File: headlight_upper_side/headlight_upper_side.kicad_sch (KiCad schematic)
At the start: 22 parts

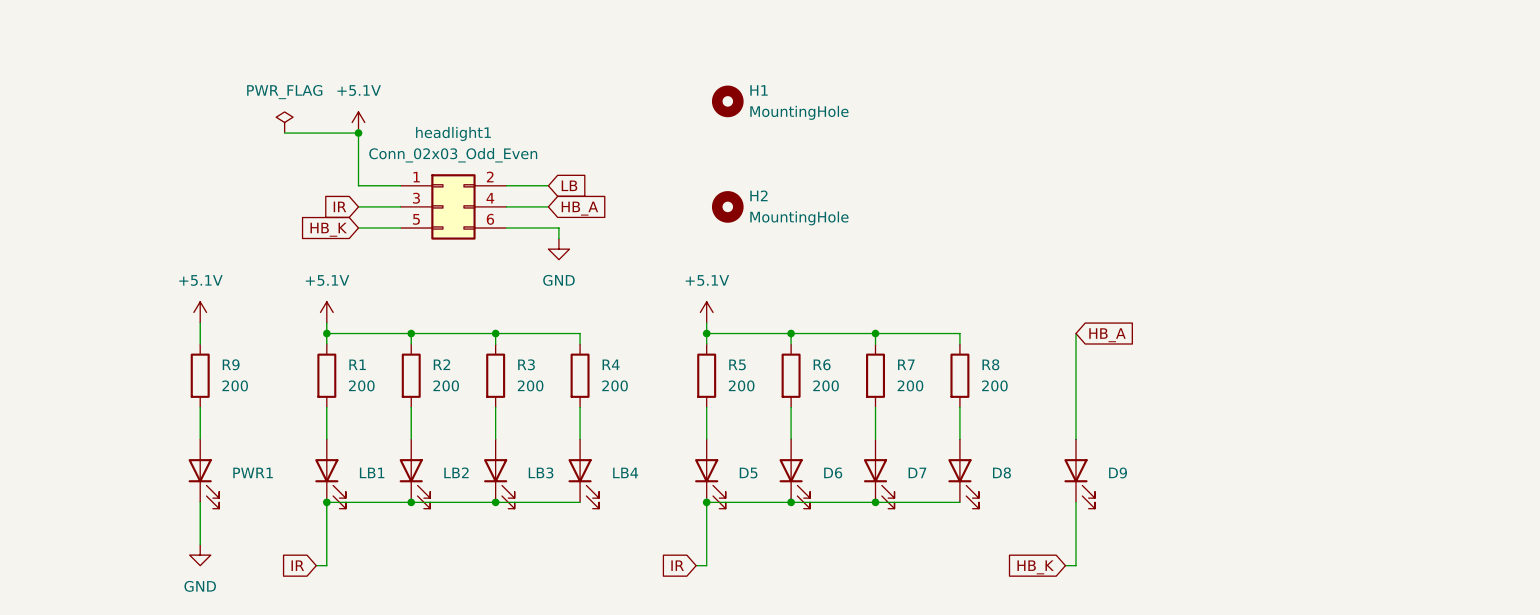
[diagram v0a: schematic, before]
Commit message: started creating headlight_upper_side
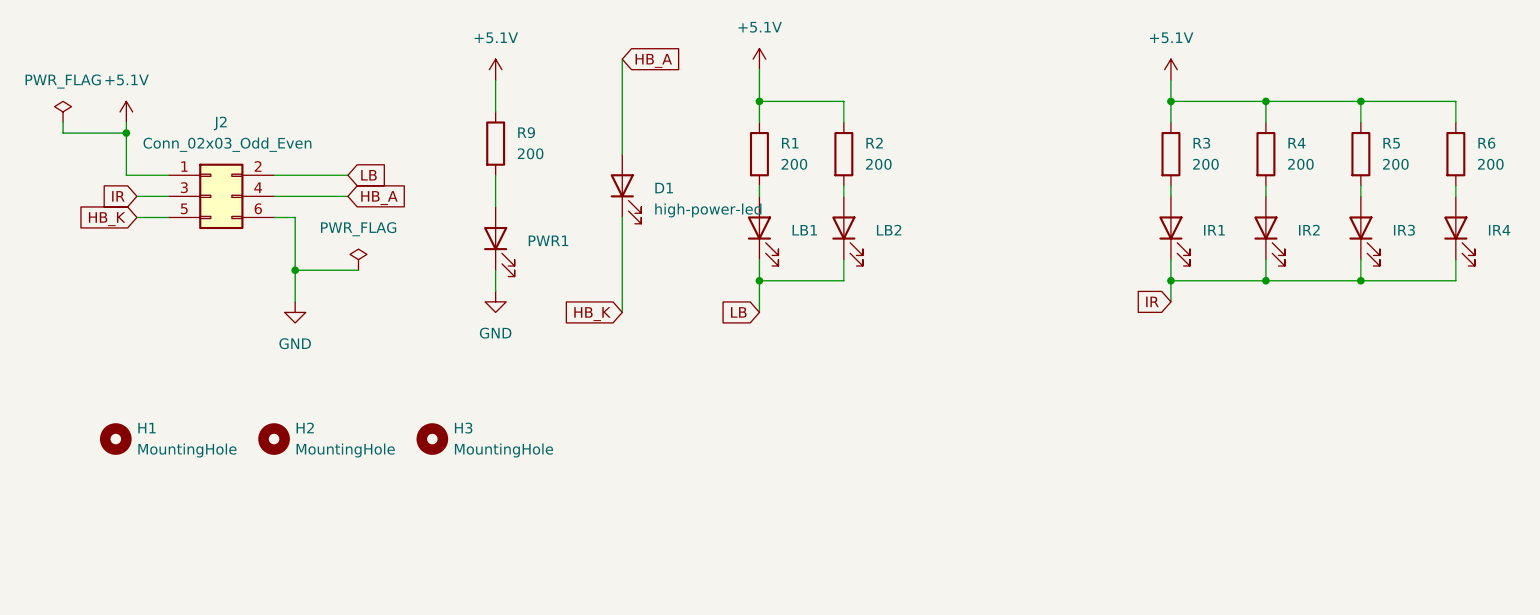
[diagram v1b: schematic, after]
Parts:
- removed D5: IR1, LED_SMD:LED_1206_3216Metric_Pad1.42x1.75mm_HandSolder, symbol Device:LED
- removed D6, D7, D8: LED, LED_SMD:LED_1206_3216Metric_Pad1.42x1.75mm_HandSolder, symbol Device:LED
- removed D9: LED, basic_parts:power led, symbol Device:LED
- removed LB3, LB4: ~, LED_SMD:LED_1206_3216Metric_Pad1.42x1.75mm_HandSolder, symbol Device:LED
- removed R7, R8: 200, Resistor_SMD:R_0603_1608Metric_Pad0.98x0.95mm_HandSolder, symbol Device:R
- removed headlight1: Conn_02x03_Odd_Even, Connector_PinHeader_2.54mm:PinHeader_2x03_P2.54mm_Vertical, symbol Connector_Generic:Conn_02x03_Odd_Even
- added D1: high-power-led, high-power-led:power led, symbol Device:LED
- added H3: MountingHole, MountingHole:MountingHole_3.2mm_M3, symbol Mechanical:MountingHole
- added IR1, IR2, IR3, IR4: ~, LED_THT:LED_D5.0mm, symbol Device:LED
- added J2: Conn_02x03_Odd_Even, Connector_PinSocket_2.54mm:PinSocket_2x03_P2.54mm_Vertical, symbol Connector_Generic:Conn_02x03_Odd_Even
- LB1, LB2: footprint LED_SMD:LED_1206_3216Metric_Pad1.42x1.75mm_HandSolder -> LED_THT:LED_D5.0mm
- PWR1: value LED -> ~; footprint LED_SMD:LED_1206_3216Metric_Pad1.42x1.75mm_HandSolder -> LED_THT:LED_D5.0mm
- R1, R2, R3, R4, R5, R6, R9: footprint Resistor_SMD:R_0603_1608Metric_Pad0.98x0.95mm_HandSolder -> Resistor_THT:R_Axial_DIN0207_L6.3mm_D2.5mm_P10.16mm_Horizontal
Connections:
- net +5.1V: now also J2.1 (Pin_1)
- net GND: now also J2.6 (Pin_6)
- net HB_A: now also D1.2 (A), J2.4 (Pin_4)
- net HB_K: now also D1.1 (K), J2.5 (Pin_5)
- net IR: now also IR1.1 (K), IR2.1 (K), IR3.1 (K), IR4.1 (K), J2.3 (Pin_3); no longer LB1.1 (K), LB2.1 (K)
- net LB: now also LB1.1 (K), LB2.1 (K), J2.2 (Pin_2)
- net at R3.2: now also IR1.2 (A)
- net at R5.2: now also IR3.2 (A)
- net at R6.2: now also IR4.2 (A)
- net at R4.2: now also IR2.2 (A)
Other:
- title: (none) -> headlight_upper_side

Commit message: 基板防水REV00発注完了
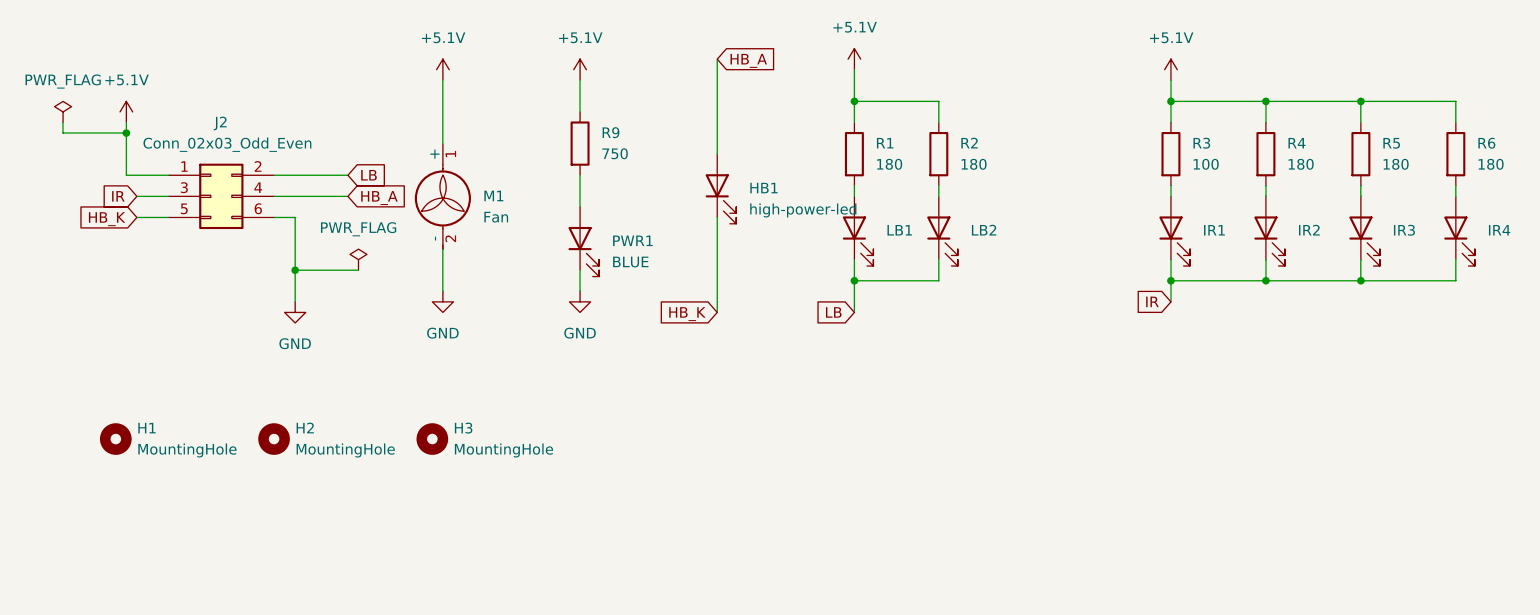
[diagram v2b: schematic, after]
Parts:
- added M1: Fan, Connector_PinHeader_2.54mm:PinHeader_1x02_P2.54mm_Vertical, symbol Motor:Fan
- HB1: renamed from D1; footprint high-power-led:power led -> specific_library:power led
- PWR1: value ~ -> BLUE; footprint LED_THT:LED_D5.0mm -> LED_SMD:LED_0805_2012Metric_Pad1.15x1.40mm_HandSolder
- R1, R2, R4, R5, R6: value 200 -> 180
- R3: value 200 -> 100
- R9: value 200 -> 750
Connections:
- net +5.1V: now also M1.1 (+)
- net GND: now also M1.2 (-)
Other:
- moved on the sheet: HB1, LB1, LB2, PWR1, R1, R2, R9
